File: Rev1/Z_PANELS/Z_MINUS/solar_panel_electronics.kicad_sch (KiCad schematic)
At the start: 24 parts, among them IC2 SM141K08TFV, IC3 SM141K04TFV, IC4 SM141K04TFV, IC5 SM141K04TFV, IC6 SM141K08TFV, U2 LTC3130EUDC-1-PBF

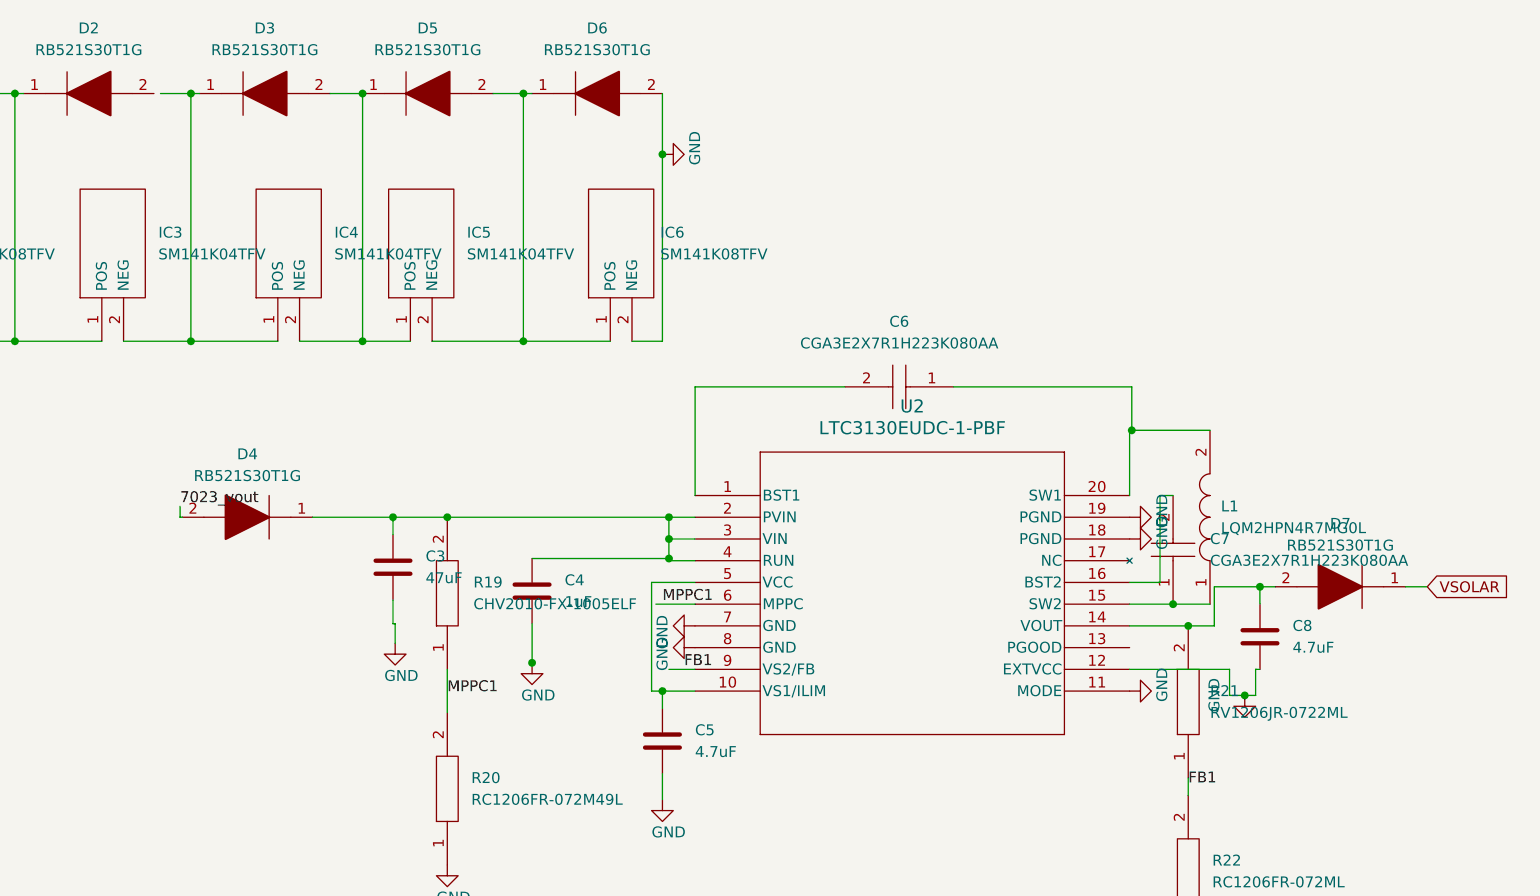
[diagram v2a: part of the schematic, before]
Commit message: finished Z minus board design
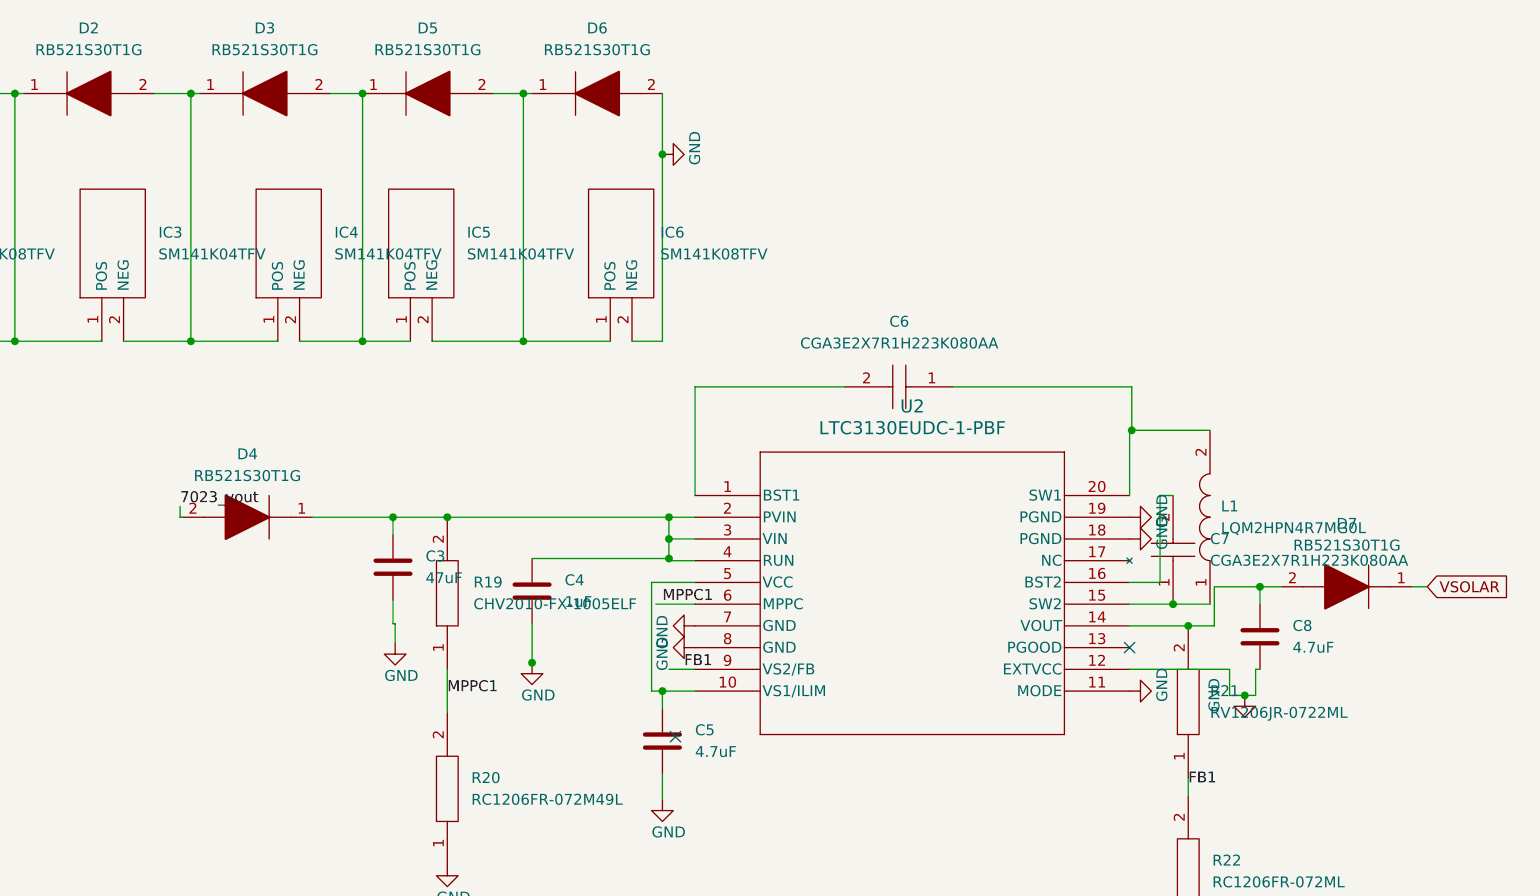
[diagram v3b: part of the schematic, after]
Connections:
- net at D3.1, IC3.2 (NEG), IC4.1 (POS): now also D2.2
- no-connect marks 0 -> 2
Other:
- moved on the sheet: D7
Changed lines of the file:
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@@
   (junction (at 118.872 106.934) (diameter 0) (color 0 0 0 0)
   )
+  (no_connect (at 135.636 115.57))
+  (no_connect (at 188.722 105.156))
   (wire (pts (xy 134.874 89.916) (xy 134.874 92.456))
     (stroke (width 0) (type default))
@@
     (stroke (width 0) (type default))
   )
-  (wire (pts (xy 203.962 98.044) (xy 205.74 98.044))
+  (wire (pts (xy 203.962 98.044) (xy 206.502 98.044))
     (stroke (width 0) (type default))
   )
@@
     (stroke (width 0) (type default))
   )
-  (wire (pts (xy 220.98 98.044) (xy 223.52 98.044))
+  (wire (pts (xy 221.742 98.044) (xy 223.52 98.044))
     (stroke (width 0) (type default))
   )
@@
     (stroke (width 0) (type default))
   )
-  (wire (pts (xy 75.438 40.386) (xy 78.994 40.386))
+  (wire (pts (xy 74.676 40.386) (xy 78.994 40.386))
     (stroke (width 0) (type default))
   )
@@
     )
   )
-  (symbol (lib_id "AA_AUTO_LOADER:RB521S30T1G") (at 220.98 98.044 180) (unit 1)
+  (symbol (lib_id "AA_AUTO_LOADER:RB521S30T1G") (at 221.742 98.044 180) (unit 1)
     (in_bom yes) (on_board yes) (dnp no) (fields_autoplaced)
-    (property "Reference" "D7" (at 213.36 90.678 0)
+    (property "Reference" "D7" (at 214.122 90.678 0)
       (effects (font (size 1.27 1.27)))
     )
-    (property "Value" "RB521S30T1G" (at 213.36 93.218 0)
+    (property "Value" "RB521S30T1G" (at 214.122 93.218 0)
       (effects (font (size 1.27 1.27)))
     )
-    (property "Footprint" "SODFL1608X70N" (at 209.55 98.044 0)
-      (effects (font (size 1.27 1.27)) (justify left) hide)
-    )
-    (property "Datasheet" "http://www.onsemi.com/pub/Collateral/RB521S30T1-D.PDF" (at 209.55 95.504 0)
-      (effects (font (size 1.27 1.27)) (justify left) hide)
-    )
-    (property "Description" "Schottky Barrier Diode" (at 209.55 92.964 0)
-      (effects (font (size 1.27 1.27)) (justify left) hide)
-    )
-    (property "Height" "0.7" (at 209.55 90.424 0)
-      (effects (font (size 1.27 1.27)) (justify left) hide)
-    )
-    (property "Manufacturer_Name" "onsemi" (at 209.55 87.884 0)
-      (effects (font (size 1.27 1.27)) (justify left) hide)
-    )
-    (property "Manufacturer_Part_Number" "RB521S30T1G" (at 209.55 85.344 0)
-      (effects (font (size 1.27 1.27)) (justify left) hide)
-    )
-    (property "Mouser Part Number" "863-RB521S30T1G" (at 209.55 82.804 0)
-      (effects (font (size 1.27 1.27)) (justify left) hide)
-    )
-    (property "Mouser Price/Stock" "https://www.mouser.co.uk/ProductDetail/onsemi/RB521S30T1G?qs=xZq1yRCsb1eKFKS8TVH%2Fqg%3D%3D" (at 209.55 80.264 0)
-      (effects (font (size 1.27 1.27)) (justify left) hide)
-    )
-    (property "Arrow Part Number" "RB521S30T1G" (at 209.55 77.724 0)
-      (effects (font (size 1.27 1.27)) (justify left) hide)
-    )
-    (property "Arrow Price/Stock" "https://www.arrow.com/en/products/rb521s30t1g/on-semiconductor?region=europe" (at 209.55 75.184 0)
-      (effects (font (size 1.27 1.27)) (justify left) hide)
-    )
+    (property "Footprint" "SODFL1608X70N" (at 210.312 98.044 0)
+      (effects (font (size 1.27 1.27)) (justify left) hide)
+    )
+    (property "Datasheet" "http://www.onsemi.com/pub/Collateral/RB521S30T1-D.PDF" (at 210.312 95.504 0)
+      (effects (font (size 1.27 1.27)) (justify left) hide)
+    )
+    (property "Description" "Schottky Barrier Diode" (at 210.312 92.964 0)
+      (effects (font (size 1.27 1.27)) (justify left) hide)
+    )
+    (property "Height" "0.7" (at 210.312 90.424 0)
+      (effects (font (size 1.27 1.27)) (justify left) hide)
+    )
+    (property "Manufacturer_Name" "onsemi" (at 210.312 87.884 0)
+      (effects (font (size 1.27 1.27)) (justify left) hide)
+    )
+    (property "Manufacturer_Part_Number" "RB521S30T1G" (at 210.312 85.344 0)
+      (effects (font (size 1.27 1.27)) (justify left) hide)
+    )
+    (property "Mouser Part Number" "863-RB521S30T1G" (at 210.312 82.804 0)
+      (effects (font (size 1.27 1.27)) (justify left) hide)
+    )
+    (property "Mouser Price/Stock" "https://www.mouser.co.uk/ProductDetail/onsemi/RB521S30T1G?qs=xZq1yRCsb1eKFKS8TVH%2Fqg%3D%3D" (at 210.312 80.264 0)
+      (effects (font (size 1.27 1.27)) (justify left) hide)
+    )
+    (property "Arrow Part Number" "RB521S30T1G" (at 210.312 77.724 0)
+      (effects (font (size 1.27 1.27)) (justify left) hide)
+    )
+    (property "Arrow Price/Stock" "https://www.arrow.com/en/products/rb521s30t1g/on-semiconductor?region=europe" (at 210.312 75.184 0)
+      (effects (font (size 1.27 1.27)) (justify left) hide)
+    )

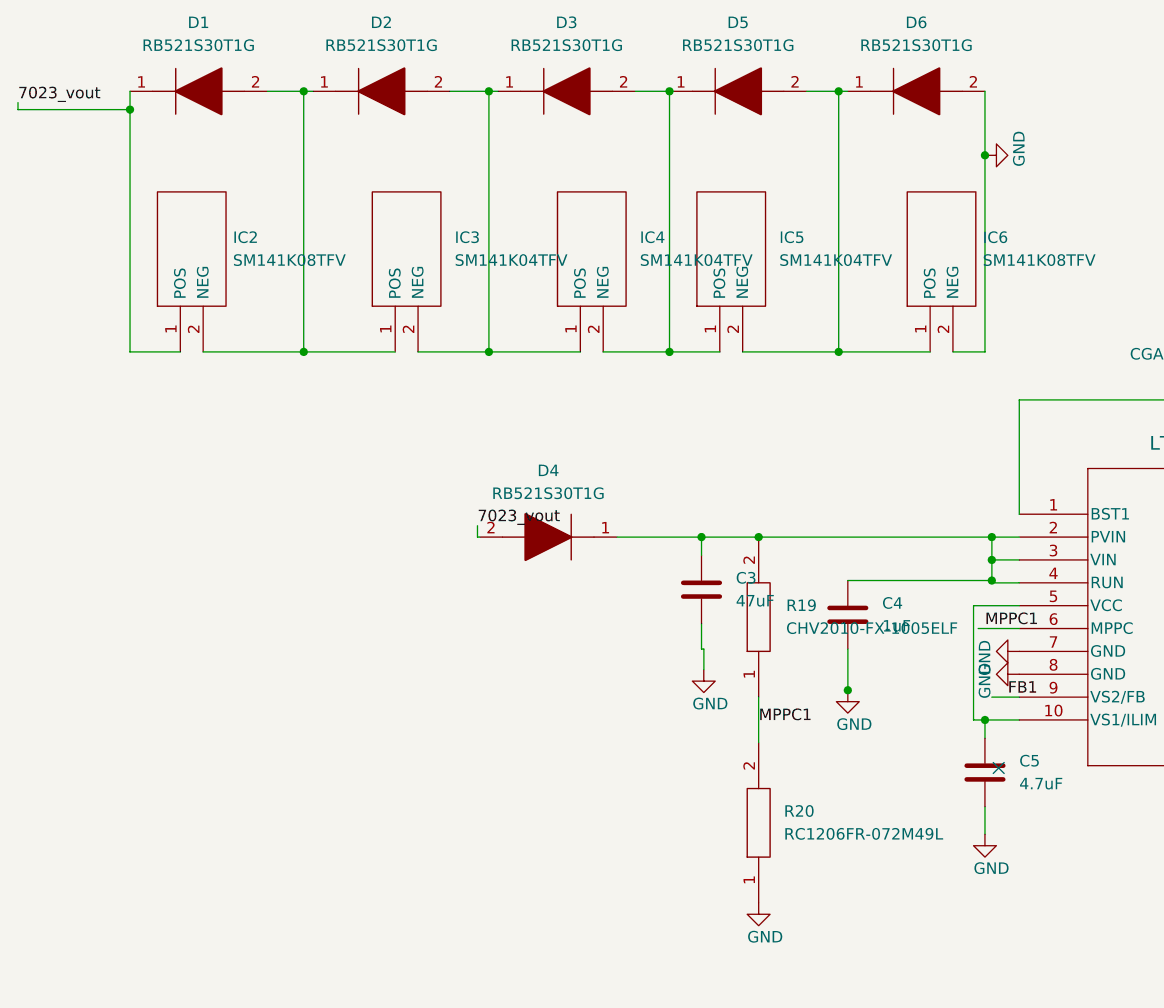
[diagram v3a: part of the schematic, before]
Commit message: CHANGED Resistor values for MPPC; added testpoints and silkscreen info
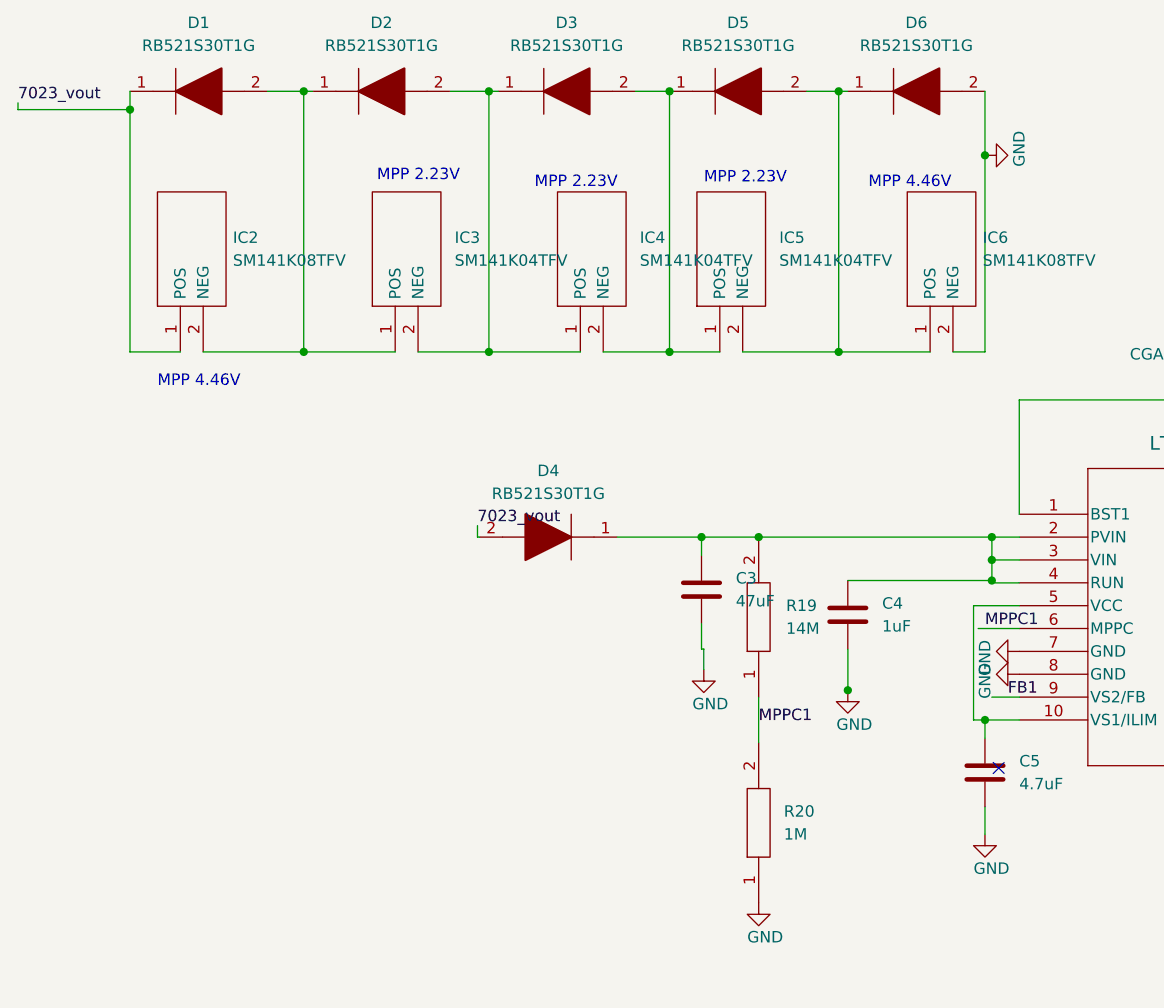
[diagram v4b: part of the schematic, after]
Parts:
- R19: value CHV2010-FX-1005ELF -> 14M
- R20: value RC1206FR-072M49L -> 1M
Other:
- note added: "MPP 2.23V"
- note added: "MPP 4.46V"
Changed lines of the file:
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@@
     (stroke (width 0) (type default))
+  )
+  (text "MPP 2.23V" (at 66.548 50.546 0)
+    (effects (font (size 1.27 1.27)) (justify left bottom))
+  )
+  (text "MPP 4.46V" (at 121.158 51.308 0)
+    (effects (font (size 1.27 1.27)) (justify left bottom))
+  )
+  (text "MPP 4.46V" (at 42.164 73.406 0)
+    (effects (font (size 1.27 1.27)) (justify left bottom))
+  )
+  (text "MPP 2.23V" (at 102.87 50.8 0)
+    (effects (font (size 1.27 1.27)) (justify left bottom))
+  )
+  (text "MPP 2.23V" (at 84.074 51.308 0)
+    (effects (font (size 1.27 1.27)) (justify left bottom))
   )
   (label "7023_vout" (at 77.724 88.646 0) (fields_autoplaced)
@@
       (effects (font (size 1.27 1.27)) (justify right))
     )
-    (property "Value" "RC1206FR-072M49L" (at 111.76 122.936 90)
+    (property "Value" "1M" (at 111.76 122.936 90)
       (effects (font (size 1.27 1.27)) (justify right))
     )
@@
       (effects (font (size 1.27 1.27)) (justify right))
     )
-    (property "Value" "CHV2010-FX-1005ELF" (at 112.014 100.076 90)
-      (effects (font (size 1.27 1.27)) (justify right))
-    )
+    (property "Value" "14M" (at 112.014 100.076 90)
+      (effects (font (size 1.27 1.27)) (justify right))
+    )

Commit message: updated boards
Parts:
- removed C3: 47uF, Capacitor_SMD:C_0805_2012Metric, symbol PCM_Capacitor_AKL:C_0805
- removed C4: 1uF, Capacitor_SMD:C_0805_2012Metric, symbol PCM_Capacitor_AKL:C_0805
- removed C6, C7: CGA3E2X7R1H223K080AA, CAPC1608X90N, symbol AA_AUTO_LOADER:CGA3E2X7R1H223K080AA
- removed D1, D2, D3, D4, D5, D6, D7: RB521S30T1G, SODFL1608X70N, symbol AA_AUTO_LOADER:RB521S30T1G
- removed R21: RV1206JR-0722ML, RESC3116X65N, symbol AA_AUTO_LOADER:RV1206JR-0722ML
- removed R22: RC1206FR-072ML, RESC3116X65N, symbol AA_AUTO_LOADER:RC1206FR-072ML
- added C10, C9: CGA3E2X7R1H223K080AA, CAPC1608X90N, symbol AA_AUTO_LOADER:CGA3E2X7R1H223K080AA
- added C11, C6: 47uF, Capacitor_SMD:C_0805_2012Metric, symbol PCM_Capacitor_AKL:C_0805
- added C7: 1uF, Capacitor_SMD:C_0805_2012Metric, symbol PCM_Capacitor_AKL:C_0805
- added D1, D2, D3, D4, D5, D6, D7: LSM115JE3_TR13, DIOM5436X330N, symbol AA_AUTO_LOADER:LSM115JE3_TR13
- R19: value 14M -> 12M
- renumbered IC6 to IC2, IC5 to IC3, IC3 to IC5, IC2 to IC6
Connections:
- net FB1 is gone; now on an unnamed net: U2.9 (VS2/FB)
- net 7023_vout: now also D5.1, D6.2
- net GND: now also U2.17 (NC), C11.2, C6.2, C7.2, D1.2
- net VSOLAR: now also D7.1
- net at IC4.1 (POS), IC5.2 (NEG): now also D3.1, D4.2
- net at IC3.1 (POS), IC4.2 (NEG): now also D2.1, D3.2
- net at IC2.1 (POS), IC3.2 (NEG): now also D1.1, D2.2
- net at L1.1, U2.15 (SW2): now also C10.1
- net at L1.2, U2.20 (SW1): now also C9.1
- net at C8.1: now also U2.10 (VS1/ILIM), U2.5 (VCC); no longer U2.14 (VOUT)
- net at IC5.1 (POS), IC6.2 (NEG): now also D4.1, D5.2
- net at U2.1 (BST1): now also C9.2
- net at R19.2, U2.2 (PVIN), U2.3 (VIN)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: now also C5.1, C6.1, C7.1, D6.1
- net at U2.16 (BST2): now also C10.2
- new net: C11.1, D7.2, U2.14 (VOUT)
- no-connect marks 2 -> 1
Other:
- moved on the sheet: IC2, IC3, IC4, IC5, IC6

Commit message: updated cap footprint
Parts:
- C11, C6: footprint Capacitor_SMD:C_0805_2012Metric -> Capacitor_SMD:C_1210_3225Metric
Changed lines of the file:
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@@
       (effects (font (size 1.27 1.27)) (justify left))
     )
-    (property "Footprint" "Capacitor_SMD:C_0805_2012Metric" (at 155.3972 54.102 0)
+    (property "Footprint" "Capacitor_SMD:C_1210_3225Metric" (at 155.3972 54.102 0)
       (effects (font (size 1.27 1.27)) hide)
     )
@@
       (effects (font (size 1.27 1.27)) (justify left))
     )
-    (property "Footprint" "Capacitor_SMD:C_0805_2012Metric" (at 256.7432 62.23 0)
-      (effects (font (size 1.27 1.27)) hide)
-    )
+    (property "Footprint" "Capacitor_SMD:C_1210_3225Metric" (at 256.7432 62.23 0)
+      (effects (font (size 1.27 1.27)) hide)
+    )
